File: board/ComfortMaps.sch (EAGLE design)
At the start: 46 parts, among them J1 PROG_HDR, U1 ADXL362, U3 ADP160-3.3, U4 MCP73833, X1 RASPI_GPIO_B+#_PIN

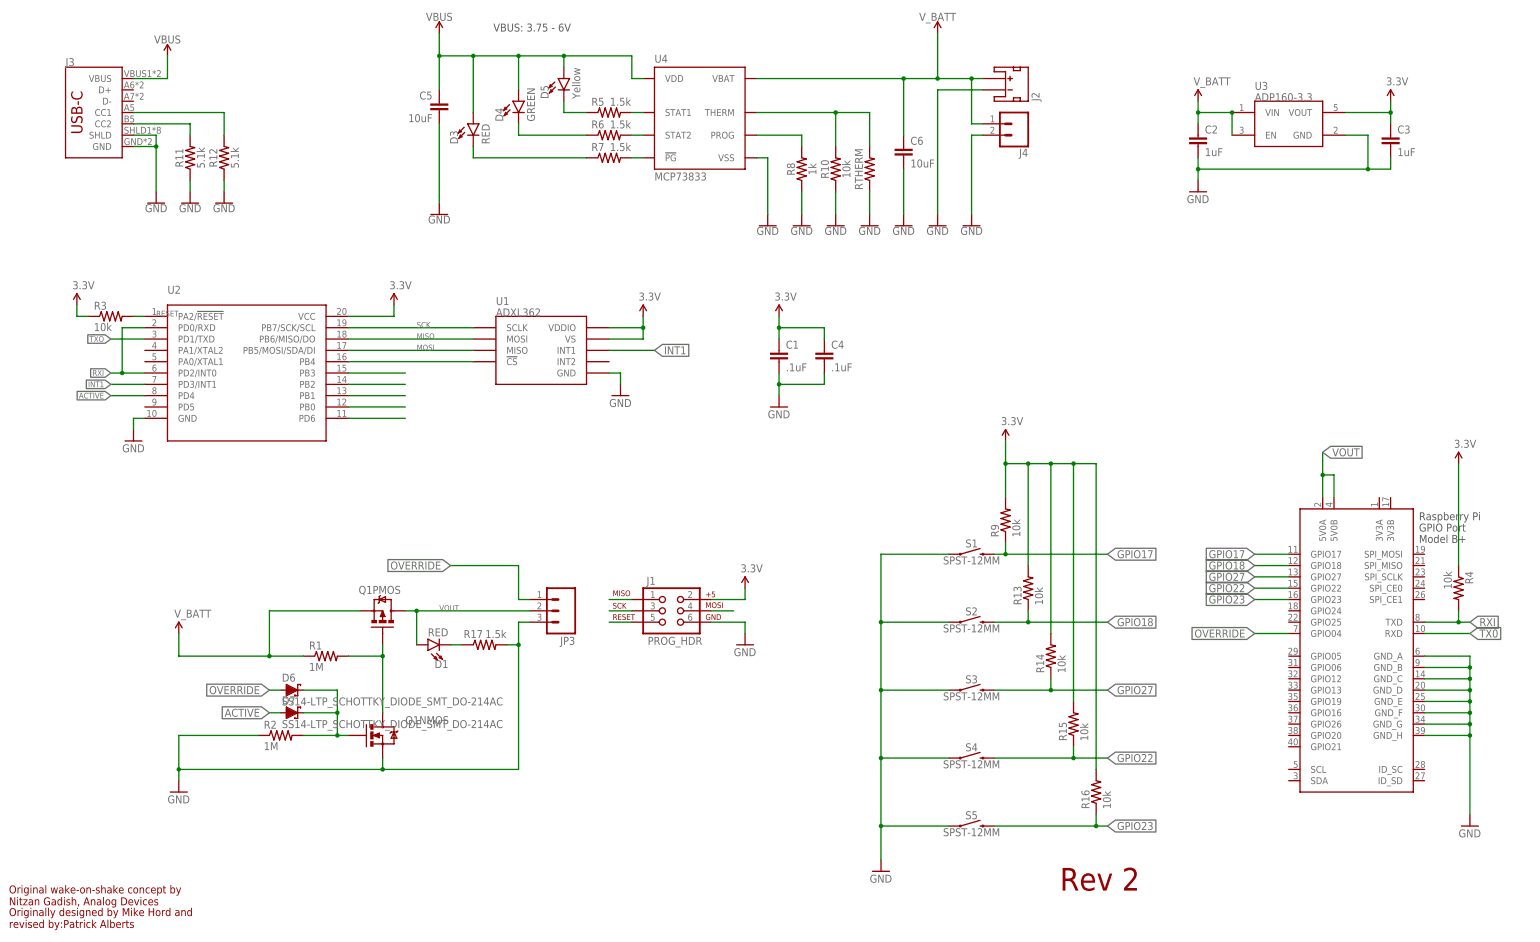
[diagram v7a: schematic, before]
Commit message: v4 of the PCB. Moved around components for better soldering, added Wake/override led, pulldown on wake.
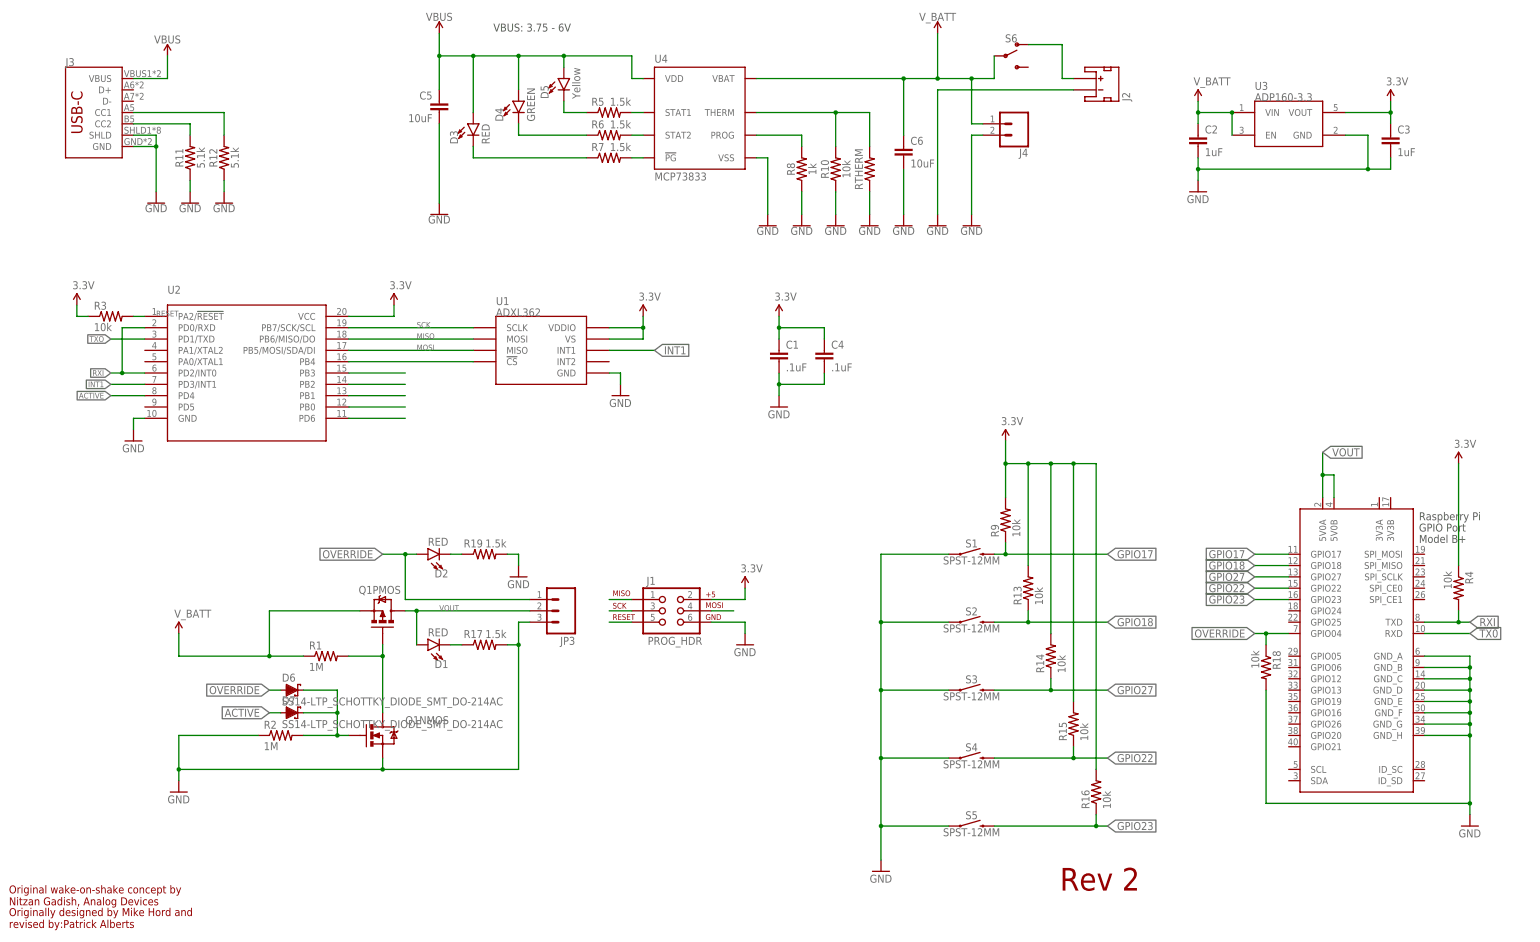
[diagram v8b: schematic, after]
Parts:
- added D2: RED, SparkFun-LED:LED-RED0603
- added R18: 10k, SparkFun-Resistors:10K-1%RES-00824
- added R19: 1.5k, SparkFun-Resistors:1.5KOHM-0603-1/10W-1%
- added S6: (no value), SparkFun-Switches:SWITCH-SPDT-SMD-RIGHT-ANGLE
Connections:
- new net N$15: J2.+, S6.O
- new net N$16: D2.C, R19.1
- net GND: now also R18.2, R19.2
- net OVERRIDE: now also D2.A, R18.1
- net V_BATT: now also S6.P; no longer J2.+
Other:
- moved on the sheet: J2
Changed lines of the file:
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@@
 <?xml version="1.0" encoding="utf-8"?>
 <!DOCTYPE eagle SYSTEM "eagle.dtd">
-<eagle version="9.5.1">
+<eagle version="9.5.2">
 <drawing>
 <settings>
@@
 <part name="D1" library="SparkFun-LED" deviceset="LED-RED" device="0603" value="RED"/>
 <part name="R17" library="SparkFun-Resistors" deviceset="1.5KOHM" device="-0603-1/10W-1%" value="1.5k"/>
+<part name="S6" library="SparkFun-Switches" library_urn="urn:adsk.eagle:library:535" deviceset="SWITCH-SPDT" device="-SMD-RIGHT-ANGLE" package3d_urn="urn:adsk.eagle:package:40179/1"/>
+<part name="R18" library="SparkFun-Resistors" deviceset="10K-1%" device="RES-00824" value="10k"/>
+<part name="D2" library="SparkFun-LED" deviceset="LED-RED" device="0603" value="RED"/>
+<part name="R19" library="SparkFun-Resistors" deviceset="1.5KOHM" device="-0603-1/10W-1%" value="1.5k"/>
+<part name="GND7" library="SparkFun-Aesthetics" deviceset="GND" device=""/>
 </parts>
 <sheets>
@@
 <attribute name="VALUE" x="187.96" y="154.686" size="1.778" layer="96" align="top-center"/>
 </instance>
-<instance part="J2" gate="G$1" x="226.06" y="185.42" smashed="yes" rot="MR90">
-<attribute name="NAME" x="231.902" y="182.88" size="1.778" layer="95" rot="MR90"/>
+<instance part="J2" gate="G$1" x="246.38" y="185.42" smashed="yes" rot="MR90">
+<attribute name="NAME" x="252.222" y="182.88" size="1.778" layer="95" rot="MR90"/>
 </instance>
 <instance part="GND15" gate="1" x="210.82" y="154.94" smashed="yes">
@@
 <attribute name="NAME" x="106.68" y="62.484" size="1.778" layer="95" font="vector" align="bottom-center"/>
 <attribute name="VALUE" x="111.76" y="62.484" size="1.778" layer="96" font="vector" rot="R180" align="top-center"/>
+</instance>
+<instance part="S6" gate="1" x="226.06" y="193.04" smashed="yes">
+<attribute name="NAME" x="227.33" y="196.088" size="1.778" layer="95" font="vector" align="bottom-center"/>
+<attribute name="VALUE" x="227.076" y="189.738" size="1.778" layer="96" font="vector" align="top-center"/>
+</instance>
+<instance part="R18" gate="G$1" x="284.48" y="55.88" smashed="yes" rot="R270">
+<attribute name="PROD_ID" x="284.48" y="55.88" size="1.778" layer="96" rot="R270" display="off"/>
+<attribute name="NAME" x="285.9786" y="59.69" size="1.778" layer="95" rot="R270"/>
+<attribute name="VALUE" x="281.178" y="59.69" size="1.778" layer="96" rot="R270"/>
+</instance>
+<instance part="D2" gate="G$1" x="96.52" y="81.28" smashed="yes" rot="R90">
+<attribute name="NAME" x="101.092" y="77.851" size="1.778" layer="95" font="vector" rot="R180"/>
+<attribute name="VALUE" x="101.092" y="83.185" size="1.778" layer="96" font="vector" rot="R180" align="top-left"/>
+</instance>
+<instance part="R19" gate="G$1" x="109.22" y="81.28" smashed="yes">
+<attribute name="NAME" x="106.68" y="82.804" size="1.778" layer="95" font="vector" align="bottom-center"/>
+<attribute name="VALUE" x="111.76" y="82.804" size="1.778" layer="96" font="vector" rot="R180" align="top-center"/>
+</instance>
+<instance part="GND7" gate="1" x="116.84" y="76.2" smashed="yes">
+<attribute name="VALUE" x="114.3" y="73.66" size="1.778" layer="96"/>
 </instance>
 </instances>
@@
 <pinref part="SUPPLY2" gate="G$1" pin="V_BATT"/>
 <wire x1="210.82" y1="198.12" x2="210.82" y2="187.96" width="0.1524" layer="91"/>
-<pinref part="J2" gate="G$1" pin="+"/>
-<wire x1="220.98" y1="187.96" x2="218.44" y2="187.96" width="0.1524" layer="91"/>
 <junction x="210.82" y="187.96"/>
 <wire x1="218.44" y1="187.96" x2="210.82" y2="187.96" width="0.1524" layer="91"/>
 <wire x1="218.44" y1="177.8" x2="218.44" y2="187.96" width="0.1524" layer="91"/>
+<pinref part="S6" gate="1" pin="P"/>
+<wire x1="218.44" y1="187.96" x2="223.52" y2="187.96" width="0.1524" layer="91"/>
+<wire x1="223.52" y1="187.96" x2="223.52" y2="193.04" width="0.1524" layer="91"/>
 <junction x="218.44" y="187.96"/>
 </segment>
@@
 <segment>
 <pinref part="J2" gate="G$1" pin="-"/>
-<wire x1="220.98" y1="185.42" x2="210.82" y2="185.42" width="0.1524" layer="91"/>
+<wire x1="241.3" y1="185.42" x2="210.82" y2="185.42" width="0.1524" layer="91"/>
 <wire x1="210.82" y1="185.42" x2="210.82" y2="157.48" width="0.1524" layer="91"/>
 <pinref part="GND15" gate="1" pin="GND"/>
@@
 <wire x1="330.2" y1="45.72" x2="330.2" y2="43.18" width="0.1524" layer="91"/>
 <wire x1="330.2" y1="43.18" x2="330.2" y2="40.64" width="0.1524" layer="91"/>
-<wire x1="330.2" y1="40.64" x2="330.2" y2="22.86" width="0.1524" layer="91"/>
+<wire x1="330.2" y1="40.64" x2="330.2" y2="25.4" width="0.1524" layer="91"/>
+<wire x1="330.2" y1="25.4" x2="330.2" y2="22.86" width="0.1524" layer="91"/>
 <wire x1="320.04" y1="55.88" x2="330.2" y2="55.88" width="0.1524" layer="91"/>
 <junction x="330.2" y="55.88"/>
@@
 <wire x1="320.04" y1="40.64" x2="330.2" y2="40.64" width="0.1524" layer="91"/>
 <junction x="330.2" y="40.64"/>
+<pinref part="R18" gate="G$1" pin="2"/>
+<wire x1="284.48" y1="50.8" x2="284.48" y2="25.4" width="0.1524" layer="91"/>
+<wire x1="284.48" y1="25.4" x2="330.2" y2="25.4" width="0.1524" layer="91"/>
+<junction x="330.2" y="25.4"/>
 </segment>
 <segment>
@@
 <junction x="198.12" y="20.32"/>
 </segment>
+<segment>
+<pinref part="R19" gate="G$1" pin="2"/>
+<wire x1="114.3" y1="81.28" x2="116.84" y2="81.28" width="0.1524" layer="91"/>
+<wire x1="116.84" y1="81.28" x2="116.84" y2="78.74" width="0.1524" layer="91"/>
+<pinref part="GND7" gate="1" pin="GND"/>
+</segment>
 </net>
 <net name="OVERRIDE" class="0">
@@
 <segment>
 <pinref part="JP3" gate="G$1" pin="1"/>
-<wire x1="119.38" y1="71.12" x2="116.84" y2="71.12" width="0.1524" layer="91"/>
-<wire x1="116.84" y1="71.12" x2="116.84" y2="78.74" width="0.1524" layer="91"/>
-<wire x1="116.84" y1="78.74" x2="101.6" y2="78.74" width="0.1524" layer="91"/>
-<label x="101.6" y="78.74" size="1.778" layer="95" rot="R180" xref="yes"/>
+<wire x1="119.38" y1="71.12" x2="91.44" y2="71.12" width="0.1524" layer="91"/>
+<wire x1="91.44" y1="71.12" x2="91.44" y2="81.28" width="0.1524" layer="91"/>
+<wire x1="91.44" y1="81.28" x2="86.36" y2="81.28" width="0.1524" layer="91"/>
+<label x="86.36" y="81.28" size="1.778" layer="95" rot="R180" xref="yes"/>
+<pinref part="D2" gate="G$1" pin="A"/>
+<wire x1="91.44" y1="81.28" x2="93.98" y2="81.28" width="0.1524" layer="91"/>
+<junction x="91.44" y="81.28"/>
 </segment>
 <segment>
 <pinref part="X1" gate="G$1" pin="GPIO04"/>
-<wire x1="289.56" y1="63.5" x2="281.94" y2="63.5" width="0.1524" layer="91"/>
+<wire x1="289.56" y1="63.5" x2="284.48" y2="63.5" width="0.1524" layer="91"/>
 <label x="281.94" y="63.5" size="1.778" layer="95" rot="R180" xref="yes"/>
+<pinref part="R18" gate="G$1" pin="1"/>
+<wire x1="284.48" y1="63.5" x2="281.94" y2="63.5" width="0.1524" layer="91"/>
+<wire x1="284.48" y1="60.96" x2="284.48" y2="63.5" width="0.1524" layer="91"/>
+<junction x="284.48" y="63.5"/>
 </segment>
 </net>
@@
 </segment>
 </net>
+<net name="N$15" class="0">
+<segment>
+<pinref part="S6" gate="1" pin="O"/>
+<wire x1="231.14" y1="195.58" x2="238.76" y2="195.58" width="0.1524" layer="91"/>
+<wire x1="238.76" y1="195.58" x2="238.76" y2="187.96" width="0.1524" layer="91"/>
+<pinref part="J2" gate="G$1" pin="+"/>
+<wire x1="238.76" y1="187.96" x2="241.3" y2="187.96" width="0.1524" layer="91"/>
+</segment>
+</net>
+<net name="N$16" class="0">
+<segment>
+<pinref part="D2" gate="G$1" pin="C"/>
+<pinref part="R19" gate="G$1" pin="1"/>
+<wire x1="101.6" y1="81.28" x2="104.14" y2="81.28" width="0.1524" layer="91"/>
+</segment>
+</net>
